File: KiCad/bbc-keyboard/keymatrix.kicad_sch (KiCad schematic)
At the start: 84 parts, among them SW1 escape, SW10 W, SW11 2, SW12 A, SW13 S, SW14 Z, SW15 f2, SW16 4, SW17 E, SW18 D, SW19 X, SW2 Q, SW20 C, SW21 space, SW22 f3, SW23 5, SW24 T, SW25 R, SW26 F, SW27 G, SW28 V, SW29 f5, SW3 F0, SW30 F4, SW31 7, SW32 6, SW33 Y, SW34 H, SW35 B, SW36 f6, SW37 8, SW38 9, SW39 U, SW4 1, SW40 J, SW41 N, SW42 M, SW43 f8, SW44 f7, SW45 I, SW46 O, SW47 K, SW48 L, SW49 <,, SW5 caps lk, SW50 f9, SW51 =-, SW52 0, SW53 P, SW54 @, SW55 ;+, SW56 >., SW57 \|, SW58 ~^, SW59 _£, SW6 shift lk, SW60 {[, SW61 *:, SW62 }], SW63 ?/, SW64 right, SW65 left, SW66 down, SW67 up, SW68 return, SW69 delete, SW7 tab, SW70 copy, SW71 shift, SW72 shift, SW73 ctrl, SW74 SW_DIP_x08, SW8 f1, SW9 3

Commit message: Break Key
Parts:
- added SW?: break, symbol Switch:SW_Push_45deg
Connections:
- new net GND: SW?.1
- new net ~{RST}: SW?.2
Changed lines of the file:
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@@
+    (stroke (width 0) (type default) (color 0 0 0 0))
+  )
+  (wire (pts (xy 35.56 26.67) (xy 55.88 26.67))
     (stroke (width 0) (type default) (color 0 0 0 0))
   )
@@
     (stroke (width 0) (type default) (color 0 0 0 0))
   )
+  (wire (pts (xy 55.88 27.94) (xy 55.88 26.67))
+    (stroke (width 0) (type default) (color 0 0 0 0))
+  )
   (wire (pts (xy 162.56 54.61) (xy 162.56 55.88))
     (stroke (width 0) (type default) (color 0 0 0 0))
@@
     (stroke (width 0) (type default) (color 0 0 0 0))
   )
+  (wire (pts (xy 49.53 33.655) (xy 49.53 34.925))
+    (stroke (width 0) (type default) (color 0 0 0 0))
+  )
   (wire (pts (xy 92.71 124.46) (xy 93.98 124.46))
     (stroke (width 0) (type default) (color 0 0 0 0))
@@
     (stroke (width 0) (type default) (color 0 0 0 0))
   )
+  (wire (pts (xy 50.8 33.655) (xy 49.53 33.655))
+    (stroke (width 0) (type default) (color 0 0 0 0))
+  )
   (wire (pts (xy 143.51 73.66) (xy 143.51 86.36))
     (stroke (width 0) (type default) (color 0 0 0 0))
@@
   )
   (bus (pts (xy 48.26 57.15) (xy 48.26 54.61))
+    (stroke (width 0) (type default) (color 0 0 0 0))
+  )
+  (wire (pts (xy 50.8 33.02) (xy 50.8 33.655))
     (stroke (width 0) (type default) (color 0 0 0 0))
   )
@@
   )
   (hierarchical_label "KC_ROW[7..0]" (shape output) (at 35.56 50.8 180)
+    (effects (font (size 1.27 1.27)) (justify right))
+  )
+  (hierarchical_label "~{RST}" (shape output) (at 35.56 26.67 180)
     (effects (font (size 1.27 1.27)) (justify right))
   )
@@
     (pin "2")
   )
+  (symbol (lib_id "Switch:SW_Push_45deg") (at 53.34 30.48 90) (unit 1)
+    (in_bom yes) (on_board yes)
+    (property "Reference" "SW?" (id 0) (at 55.88 29.21 90)
+      (effects (font (size 1.27 1.27)) (justify right))
+    )
+    (property "Value" "break" (id 1) (at 53.34 34.29 90)
+      (effects (font (size 1.27 1.27)) (justify right))
+    )
+    (property "Footprint" "" (id 2) (at 53.34 30.48 0)
+      (effects (font (size 1.27 1.27)) hide)
+    )
+    (property "Datasheet" "~" (id 3) (at 53.34 30.48 0)
+      (effects (font (size 1.27 1.27)) hide)
+    )
+    (pin "1")
+    (pin "2")
+  )
   (symbol (lib_id "Switch:SW_Push_45deg") (at 109.22 121.92 90) (unit 1)
     (in_bom yes) (on_board yes)
@@
     (pin "2")
   )
+  (symbol (lib_id "power:GND") (at 49.53 34.925 0) (unit 1)
+    (in_bom yes) (on_board yes) (fields_autoplaced)
+    (property "Reference" "#PWR?" (id 0) (at 49.53 41.275 0)
+      (effects (font (size 1.27 1.27)) hide)
+    )
+    (property "Value" "GND" (id 1) (at 49.53 39.37 0))
+    (property "Footprint" "" (id 2) (at 49.53 34.925 0)
+      (effects (font (size 1.27 1.27)) hide)
+    )
+    (property "Datasheet" "" (id 3) (at 49.53 34.925 0)
+      (effects (font (size 1.27 1.27)) hide)
+    )
+    (pin "1")
+  )
   (symbol (lib_id "Switch:SW_Push_45deg") (at 185.42 83.82 90) (unit 1)

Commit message: All keys laid out
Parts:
- gave numbers to parts that had none: 1
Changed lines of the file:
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@@
   (symbol (lib_id "Switch:SW_Push_45deg") (at 53.34 30.48 90) (unit 1)
     (in_bom yes) (on_board yes)
-    (property "Reference" "SW?" (id 0) (at 55.88 29.21 90)
+    (property "Reference" "SW75" (id 0) (at 55.88 29.21 90)
       (effects (font (size 1.27 1.27)) (justify right))
     )
@@
   (symbol (lib_id "power:GND") (at 49.53 34.925 0) (unit 1)
     (in_bom yes) (on_board yes) (fields_autoplaced)
-    (property "Reference" "#PWR?" (id 0) (at 49.53 41.275 0)
-      (effects (font (size 1.27 1.27)) hide)
-    )
+    (property "Reference" "#PWR0110" (id 0) (at 49.53 41.275 0)
+      (effects (font (size 1.27 1.27)) hide)
+    )

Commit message: missing .sch updates
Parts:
- SW1, SW10, SW11, SW12, SW13, SW14, SW15, SW16, SW17, SW18, SW19, SW2, SW20, SW22, SW23, SW24, SW25, SW26, SW27, SW28, SW29, SW3, SW30, SW31, SW32, SW33, SW34, SW35, SW36, SW37, SW38, SW39, SW4, SW40, SW41, SW42, SW43, SW44, SW45, SW46, SW47, SW48, SW49, SW5, SW50, SW51, SW52, SW53, SW54, SW55, SW56, SW57, SW58, SW59, SW6, SW60, SW61, SW62, SW63, SW64, SW65, SW66, SW67, SW69, SW70, SW73, SW75, SW8, SW9: footprint (none) -> Switch_Keyboard_Cherry_MX:SW_Cherry_MX_PCB_1.00u
- SW21: footprint (none) -> Switch_Keyboard_Cherry_MX:SW_Cherry_MX_PCB_6.50u
- SW68: footprint (none) -> Switch_Keyboard_Cherry_MX:SW_Cherry_MX_PCB_2.00u
- SW7, SW71, SW72: footprint (none) -> Switch_Keyboard_Cherry_MX:SW_Cherry_MX_PCB_1.50u

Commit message: placing components
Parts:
- D1, D10, D2, D3, D4, D5, D6, D7, D8, D9: footprint (none) -> Diode_THT:D_DO-34_SOD68_P12.70mm_Horizontal
- SW74: footprint (none) -> Button_Switch_THT:SW_DIP_SPSTx08_Slide_9.78x22.5mm_W7.62mm_P2.54mm
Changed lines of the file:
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@@
       (effects (font (size 1.27 1.27)) (justify left))
     )
-    (property "Footprint" "" (id 2) (at 154.94 160.02 0)
+    (property "Footprint" "Button_Switch_THT:SW_DIP_SPSTx08_Slide_9.78x22.5mm_W7.62mm_P2.54mm" (id 2) (at 154.94 160.02 0)
       (effects (font (size 1.27 1.27)) hide)
     )
@@
       (effects (font (size 1.27 1.27)) (justify left))
     )
-    (property "Footprint" "" (id 2) (at 130.81 143.51 0)
+    (property "Footprint" "Diode_THT:D_DO-34_SOD68_P12.70mm_Horizontal" (id 2) (at 130.81 143.51 0)
       (effects (font (size 1.27 1.27)) hide)
     )
@@
       (effects (font (size 1.27 1.27)) (justify left))
     )
-    (property "Footprint" "" (id 2) (at 194.31 143.51 0)
+    (property "Footprint" "Diode_THT:D_DO-34_SOD68_P12.70mm_Horizontal" (id 2) (at 194.31 143.51 0)
       (effects (font (size 1.27 1.27)) hide)
     )
@@
       (effects (font (size 1.27 1.27)) (justify left))
     )
-    (property "Footprint" "" (id 2) (at 156.21 143.51 0)
+    (property "Footprint" "Diode_THT:D_DO-34_SOD68_P12.70mm_Horizontal" (id 2) (at 156.21 143.51 0)
       (effects (font (size 1.27 1.27)) hide)
     )
@@
       (effects (font (size 1.27 1.27)) (justify left))
     )
-    (property "Footprint" "" (id 2) (at 105.41 143.51 0)
+    (property "Footprint" "Diode_THT:D_DO-34_SOD68_P12.70mm_Horizontal" (id 2) (at 105.41 143.51 0)
       (effects (font (size 1.27 1.27)) hide)
     )
@@
       (effects (font (size 1.27 1.27)) (justify left))
     )
-    (property "Footprint" "" (id 2) (at 80.01 143.51 0)
+    (property "Footprint" "Diode_THT:D_DO-34_SOD68_P12.70mm_Horizontal" (id 2) (at 80.01 143.51 0)
       (effects (font (size 1.27 1.27)) hide)
     )
@@
       (effects (font (size 1.27 1.27)) (justify left))
     )
-    (property "Footprint" "" (id 2) (at 181.61 143.51 0)
+    (property "Footprint" "Diode_THT:D_DO-34_SOD68_P12.70mm_Horizontal" (id 2) (at 181.61 143.51 0)
       (effects (font (size 1.27 1.27)) hide)
     )
@@
       (effects (font (size 1.27 1.27)) (justify left))
     )
-    (property "Footprint" "" (id 2) (at 92.71 143.51 0)
+    (property "Footprint" "Diode_THT:D_DO-34_SOD68_P12.70mm_Horizontal" (id 2) (at 92.71 143.51 0)
       (effects (font (size 1.27 1.27)) hide)
     )
@@
       (effects (font (size 1.27 1.27)) (justify left))
     )
-    (property "Footprint" "" (id 2) (at 168.91 143.51 0)
+    (property "Footprint" "Diode_THT:D_DO-34_SOD68_P12.70mm_Horizontal" (id 2) (at 168.91 143.51 0)
       (effects (font (size 1.27 1.27)) hide)
     )
@@
       (effects (font (size 1.27 1.27)) (justify left))
     )
-    (property "Footprint" "" (id 2) (at 143.51 143.51 0)
+    (property "Footprint" "Diode_THT:D_DO-34_SOD68_P12.70mm_Horizontal" (id 2) (at 143.51 143.51 0)
       (effects (font (size 1.27 1.27)) hide)
     )
@@
       (effects (font (size 1.27 1.27)) (justify left))
     )
-    (property "Footprint" "" (id 2) (at 118.11 143.51 0)
-      (effects (font (size 1.27 1.27)) hide)
-    )
+    (property "Footprint" "Diode_THT:D_DO-34_SOD68_P12.70mm_Horizontal" (id 2) (at 118.11 143.51 0)
+      (effects (font (size 1.27 1.27)) hide)
+    )

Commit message: start routing
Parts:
- D1, D10, D2, D3, D4, D5, D6, D7, D8, D9: footprint Diode_THT:D_DO-34_SOD68_P12.70mm_Horizontal -> Diode_THT:D_DO-34_SOD68_P10.16mm_Horizontal
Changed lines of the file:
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@@
       (effects (font (size 1.27 1.27)) (justify left))
     )
-    (property "Footprint" "Diode_THT:D_DO-34_SOD68_P12.70mm_Horizontal" (id 2) (at 130.81 143.51 0)
+    (property "Footprint" "Diode_THT:D_DO-34_SOD68_P10.16mm_Horizontal" (id 2) (at 130.81 143.51 0)
       (effects (font (size 1.27 1.27)) hide)
     )
@@
       (effects (font (size 1.27 1.27)) (justify left))
     )
-    (property "Footprint" "Diode_THT:D_DO-34_SOD68_P12.70mm_Horizontal" (id 2) (at 194.31 143.51 0)
+    (property "Footprint" "Diode_THT:D_DO-34_SOD68_P10.16mm_Horizontal" (id 2) (at 194.31 143.51 0)
       (effects (font (size 1.27 1.27)) hide)
     )
@@
       (effects (font (size 1.27 1.27)) (justify left))
     )
-    (property "Footprint" "Diode_THT:D_DO-34_SOD68_P12.70mm_Horizontal" (id 2) (at 156.21 143.51 0)
+    (property "Footprint" "Diode_THT:D_DO-34_SOD68_P10.16mm_Horizontal" (id 2) (at 156.21 143.51 0)
       (effects (font (size 1.27 1.27)) hide)
     )
@@
       (effects (font (size 1.27 1.27)) (justify left))
     )
-    (property "Footprint" "Diode_THT:D_DO-34_SOD68_P12.70mm_Horizontal" (id 2) (at 105.41 143.51 0)
+    (property "Footprint" "Diode_THT:D_DO-34_SOD68_P10.16mm_Horizontal" (id 2) (at 105.41 143.51 0)
       (effects (font (size 1.27 1.27)) hide)
     )
@@
       (effects (font (size 1.27 1.27)) (justify left))
     )
-    (property "Footprint" "Diode_THT:D_DO-34_SOD68_P12.70mm_Horizontal" (id 2) (at 80.01 143.51 0)
+    (property "Footprint" "Diode_THT:D_DO-34_SOD68_P10.16mm_Horizontal" (id 2) (at 80.01 143.51 0)
       (effects (font (size 1.27 1.27)) hide)
     )
@@
       (effects (font (size 1.27 1.27)) (justify left))
     )
-    (property "Footprint" "Diode_THT:D_DO-34_SOD68_P12.70mm_Horizontal" (id 2) (at 181.61 143.51 0)
+    (property "Footprint" "Diode_THT:D_DO-34_SOD68_P10.16mm_Horizontal" (id 2) (at 181.61 143.51 0)
       (effects (font (size 1.27 1.27)) hide)
     )
@@
       (effects (font (size 1.27 1.27)) (justify left))
     )
-    (property "Footprint" "Diode_THT:D_DO-34_SOD68_P12.70mm_Horizontal" (id 2) (at 92.71 143.51 0)
+    (property "Footprint" "Diode_THT:D_DO-34_SOD68_P10.16mm_Horizontal" (id 2) (at 92.71 143.51 0)
       (effects (font (size 1.27 1.27)) hide)
     )
@@
       (effects (font (size 1.27 1.27)) (justify left))
     )
-    (property "Footprint" "Diode_THT:D_DO-34_SOD68_P12.70mm_Horizontal" (id 2) (at 168.91 143.51 0)
+    (property "Footprint" "Diode_THT:D_DO-34_SOD68_P10.16mm_Horizontal" (id 2) (at 168.91 143.51 0)
       (effects (font (size 1.27 1.27)) hide)
     )
@@
       (effects (font (size 1.27 1.27)) (justify left))
     )
-    (property "Footprint" "Diode_THT:D_DO-34_SOD68_P12.70mm_Horizontal" (id 2) (at 143.51 143.51 0)
+    (property "Footprint" "Diode_THT:D_DO-34_SOD68_P10.16mm_Horizontal" (id 2) (at 143.51 143.51 0)
       (effects (font (size 1.27 1.27)) hide)
     )
@@
       (effects (font (size 1.27 1.27)) (justify left))
     )
-    (property "Footprint" "Diode_THT:D_DO-34_SOD68_P12.70mm_Horizontal" (id 2) (at 118.11 143.51 0)
-      (effects (font (size 1.27 1.27)) hide)
-    )
+    (property "Footprint" "Diode_THT:D_DO-34_SOD68_P10.16mm_Horizontal" (id 2) (at 118.11 143.51 0)
+      (effects (font (size 1.27 1.27)) hide)
+    )

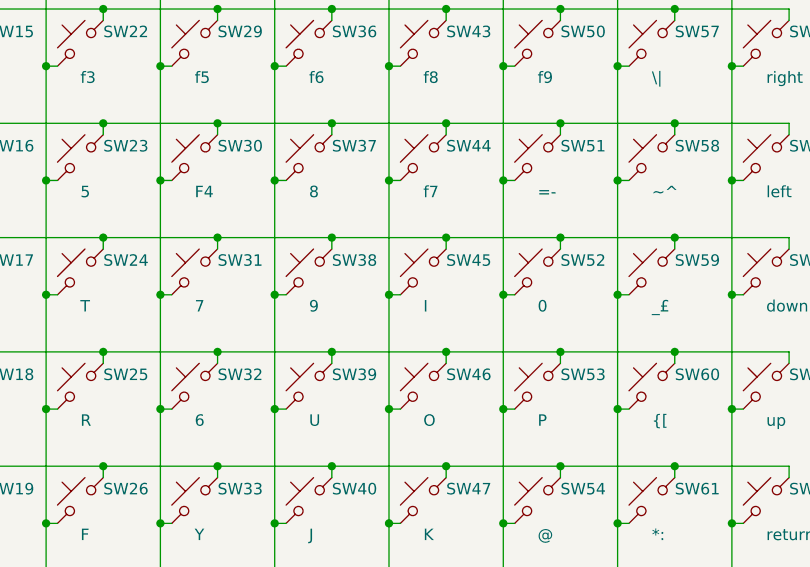
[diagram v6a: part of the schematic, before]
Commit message: FIX: I/9 were swapped blame AUG
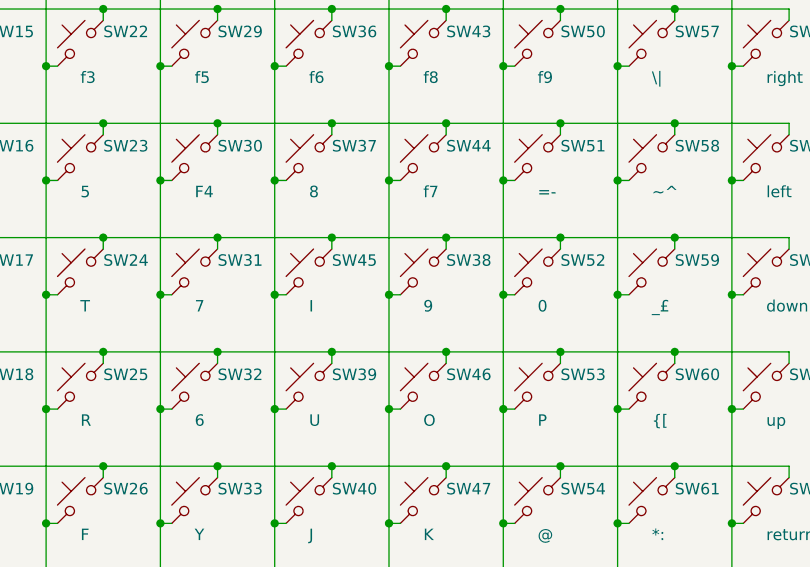
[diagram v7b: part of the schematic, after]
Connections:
- net KC_COL5: now also SW45.1; no longer SW38.1
- net KC_COL6: now also SW38.1; no longer SW45.1
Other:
- moved on the sheet: SW38, SW45
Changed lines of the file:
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@@
     (pin "2")
   )
-  (symbol (lib_id "Switch:SW_Push_45deg") (at 160.02 83.82 90) (unit 1)
-    (in_bom yes) (on_board yes)
-    (property "Reference" "SW45" (id 0) (at 162.56 82.55 90)
-      (effects (font (size 1.27 1.27)) (justify right))
-    )
-    (property "Value" "I" (id 1) (at 160.02 87.63 90)
-      (effects (font (size 1.27 1.27)) (justify right))
-    )
-    (property "Footprint" "Switch_Keyboard_Cherry_MX:SW_Cherry_MX_PCB_1.00u" (id 2) (at 160.02 83.82 0)
-      (effects (font (size 1.27 1.27)) hide)
-    )
-    (property "Datasheet" "~" (id 3) (at 160.02 83.82 0)
+  (symbol (lib_id "Switch:SW_Push_45deg") (at 147.32 83.82 90) (unit 1)
+    (in_bom yes) (on_board yes)
+    (property "Reference" "SW45" (id 0) (at 149.86 82.55 90)
+      (effects (font (size 1.27 1.27)) (justify right))
+    )
+    (property "Value" "I" (id 1) (at 147.32 87.63 90)
+      (effects (font (size 1.27 1.27)) (justify right))
+    )
+    (property "Footprint" "Switch_Keyboard_Cherry_MX:SW_Cherry_MX_PCB_1.00u" (id 2) (at 147.32 83.82 0)
+      (effects (font (size 1.27 1.27)) hide)
+    )
+    (property "Datasheet" "~" (id 3) (at 147.32 83.82 0)
       (effects (font (size 1.27 1.27)) hide)
     )
@@
     (pin "2")
   )
-  (symbol (lib_id "Switch:SW_Push_45deg") (at 147.32 83.82 90) (unit 1)
-    (in_bom yes) (on_board yes)
-    (property "Reference" "SW38" (id 0) (at 149.86 82.55 90)
-      (effects (font (size 1.27 1.27)) (justify right))
-    )
-    (property "Value" "9" (id 1) (at 147.32 87.63 90)
-      (effects (font (size 1.27 1.27)) (justify right))
-    )
-    (property "Footprint" "Switch_Keyboard_Cherry_MX:SW_Cherry_MX_PCB_1.00u" (id 2) (at 147.32 83.82 0)
-      (effects (font (size 1.27 1.27)) hide)
-    )
-    (property "Datasheet" "~" (id 3) (at 147.32 83.82 0)
-      (effects (font (size 1.27 1.27)) hide)
-    )
+  (symbol (lib_id "Switch:SW_Push_45deg") (at 160.02 83.82 90) (unit 1)
+    (in_bom yes) (on_board yes)
+    (property "Reference" "SW38" (id 0) (at 162.56 82.55 90)
+      (effects (font (size 1.27 1.27)) (justify right))
+    )
+    (property "Value" "9" (id 1) (at 160.02 87.63 90)
+      (effects (font (size 1.27 1.27)) (justify right))
+    )
+    (property "Footprint" "Switch_Keyboard_Cherry_MX:SW_Cherry_MX_PCB_1.00u" (id 2) (at 160.02 83.82 0)
+      (effects (font (size 1.27 1.27)) hide)
+    )
+    (property "Datasheet" "~" (id 3) (at 160.02 83.82 0)
+      (effects (font (size 1.27 1.27)) hide)
+    )
